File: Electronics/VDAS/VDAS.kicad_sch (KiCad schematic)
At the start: 7 parts, among them U1 AD5445YRUZ, U2 AD5445YRUZ, U3 AMC1303E2520DWV, U4 AMC1303E2520DWV, U5 MAX11102AUB+, U6 MAX11102AUB+, U7 ADA4851-4YRUZ

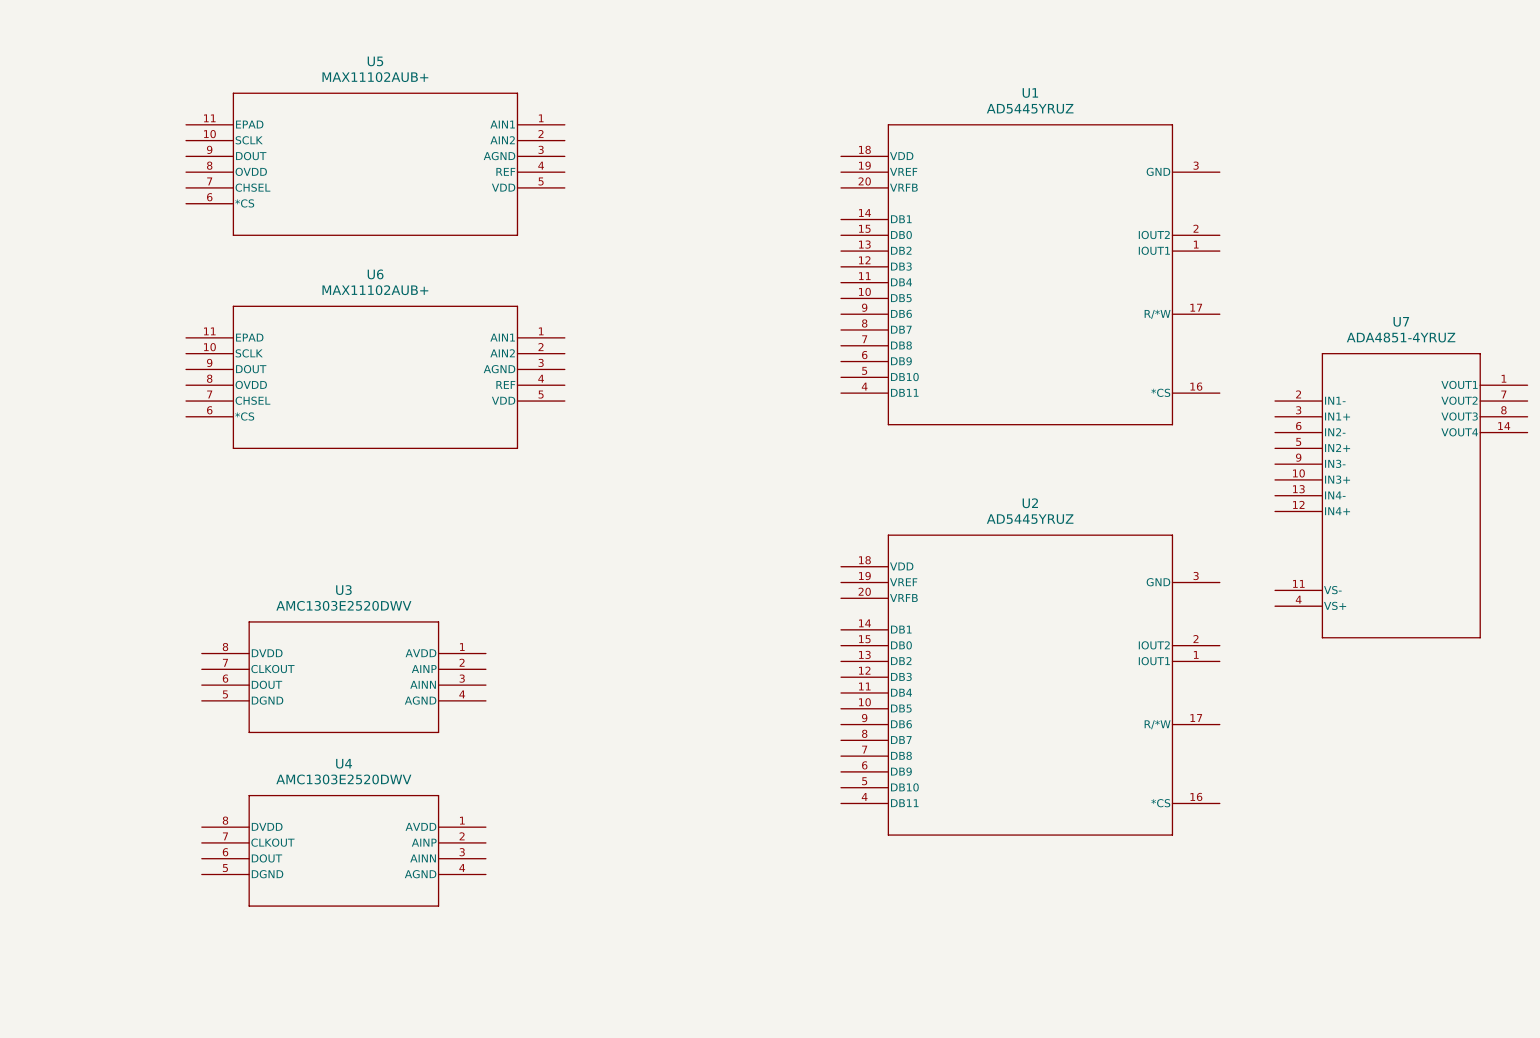
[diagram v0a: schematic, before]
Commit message: Major changes
- Modified schematic
- Added functionalities to GUI
- Updated FW
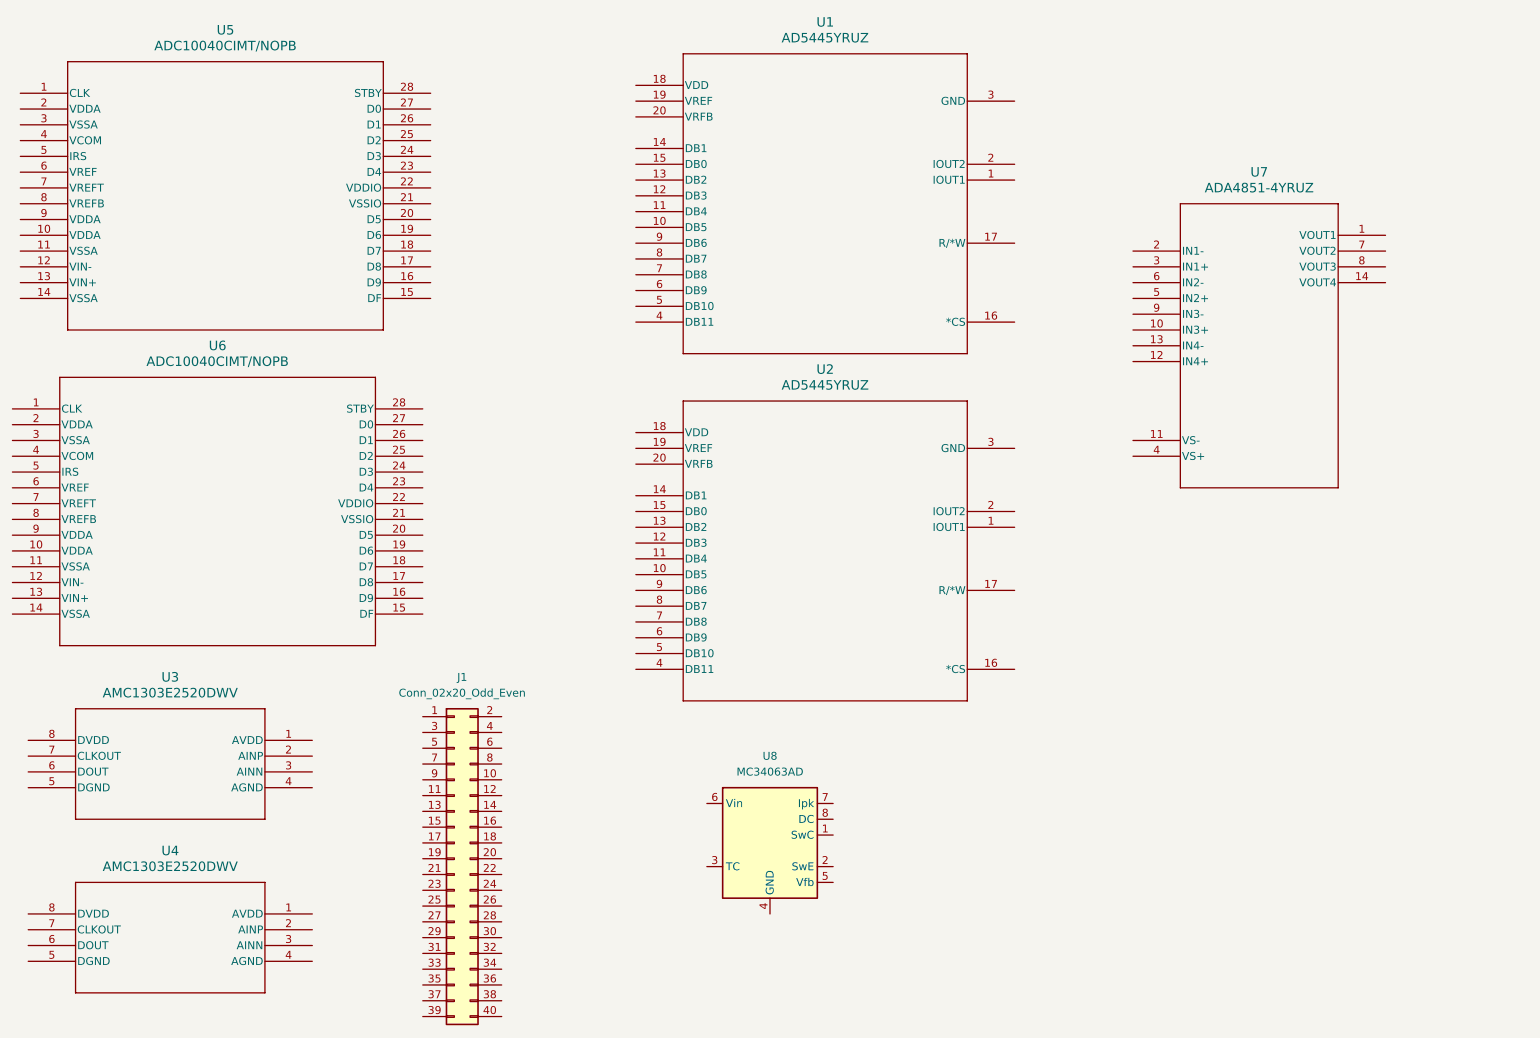
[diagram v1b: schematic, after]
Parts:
- removed U5, U6: MAX11102AUB+, 21-0109D_MXM, symbol MAX11102AUB:MAX11102AUB+
- added J1: Conn_02x20_Odd_Even, symbol Connector_Generic:Conn_02x20_Odd_Even
- added U5, U6: ADC10040CIMT/NOPB, MTC28, symbol ADC10040:ADC10040CIMT_NOPB
- added U8: MC34063AD, Package_SO:SOIC-8_3.9x4.9mm_P1.27mm, symbol Regulator_Switching:MC34063AD
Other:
- moved on the sheet: U1, U2, U3, U4, U7
